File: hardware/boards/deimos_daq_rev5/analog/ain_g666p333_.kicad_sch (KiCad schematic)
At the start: 6 parts, among them IC36001 INA826AIDR

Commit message: restore rev5 and make this rev rev6
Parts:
- removed C34003, C34004: 0.1uF, Capacitor_SMD:C_0402_1005Metric, symbol Device:C_Small
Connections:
- net +1V024 is gone; now on net GND: IC36001.6 (REF)
- net -12V is gone; now on net GND: IC36001.5 (-VS)
- net +12V renamed +3V3
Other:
- note added: "G = 1 + (49.4k / Rg) = 1 + (49.4k / 75) = 666 + 1/3"
- note removed: "G = 1 + (49.4k / Rg) = 1 + (49.4k / 75) = 659+2/3"
- moved on the sheet: C36001

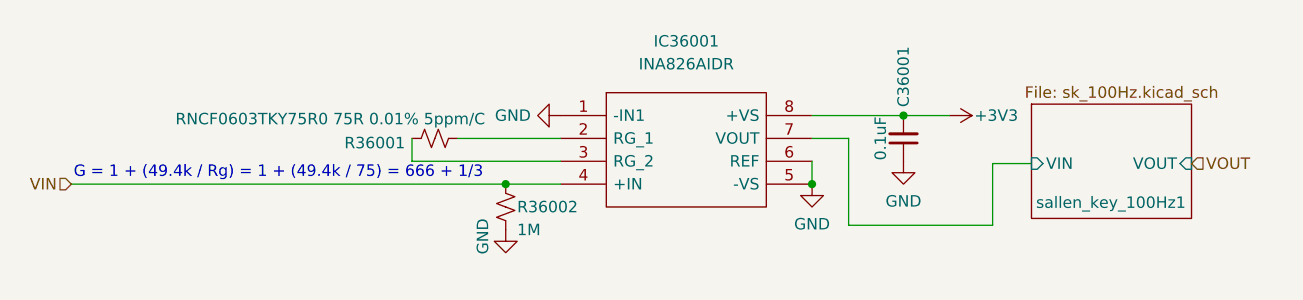
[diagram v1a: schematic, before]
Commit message: put +/12V on all inamps. add 3.3V zener behind first resistor of each filter.
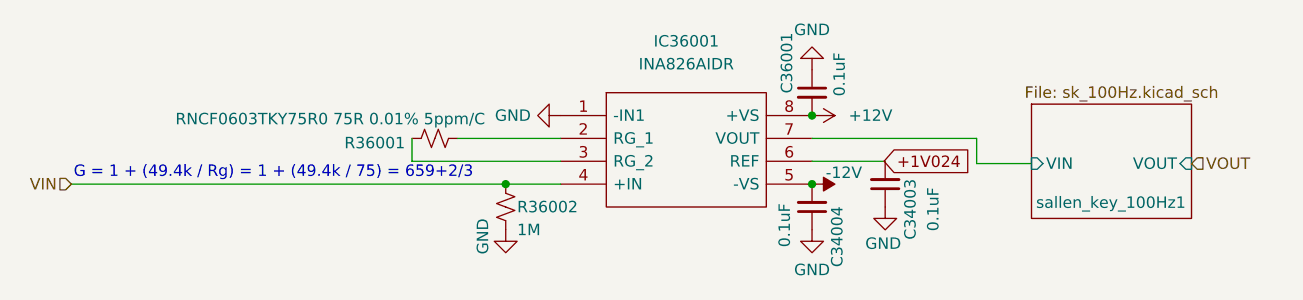
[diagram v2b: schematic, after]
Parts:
- added C34003, C34004: 0.1uF, Capacitor_SMD:C_0402_1005Metric, symbol Device:C_Small
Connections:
- net GND: now also C34003.1, C34004.1; no longer IC36001.5 (-VS), IC36001.6 (REF)
- net +3V3 renamed +12V
- new net +1V024: C34003.2, IC36001.6 (REF)
- new net -12V: C34004.2, IC36001.5 (-VS)
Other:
- note added: "G = 1 + (49.4k / Rg) = 1 + (49.4k / 75) = 659+2/3"
- note removed: "G = 1 + (49.4k / Rg) = 1 + (49.4k / 75) = 666 + 1/3"
- moved on the sheet: C36001
